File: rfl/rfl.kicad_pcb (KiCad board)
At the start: 4 copper layers, 20 x 30 mm, 35 parts, among them J1 636101111001, J2 Conn_01x09, J801 629722000214, J802 swd, U1 SX1281, U2 STM32G0B1KETxN, U3 TPS7A19, U801 USBLC6-2SC6, Y1 52MHz

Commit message: before switch
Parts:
- added C15: C, Capacitor_SMD:C_0402_1005Metric, F.Cu at (176.8, 87.3)
- added R5: R, Resistor_SMD:R_0402_1005Metric, F.Cu at (182.7, 76.5)
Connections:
- U2 pad 24: /swdclk -> /swdio
- U2 pad 25: /swdio -> /swdclk
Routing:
- net /nreset: track 8.20 -> 13.2 mm, vias 1 -> 2
- net /swdclk: track 6.42 -> 10.9 mm
- net /swdio: track 7.61 -> 8.32 mm
- net +3.3V: track 11.3 -> 11.0 mm, vias 11 -> 12
- net GND: vias 107 -> 104

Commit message: v2 with rf switch wip
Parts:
- removed C11, C12: C, Capacitor_SMD:C_0402_1005Metric
- removed L3, L4: L, Inductor_SMD:L_0402_1005Metric
- added C8: C, Capacitor_SMD:C_0603_1608Metric, F.Cu at (210.5, 77.7)
- added D3: D_TVS, Diode_SMD:D_0402_1005Metric, F.Cu at (218.0, 91.7)
- added D4: D_TVS, Diode_SMD:D_0402_1005Metric, F.Cu at (221.9, 91.7)
- added D5: D_TVS, Diode_SMD:D_0402_1005Metric, F.Cu at (210.0, 91.7)
- added D6: D_TVS, Diode_SMD:D_0402_1005Metric, F.Cu at (214.1, 91.7)
- added FL1: 2450FM07D0034001T, rfl-lib-fp:2450FM07D0034001T, F.Cu at (214.2, 77.5)
- added J3: 636101111001, Connector_Coaxial:U.FL_Hirose_U.FL-R-SMT-1_Vertical, F.Cu at (211.5, 69.8)
- added R10: R, Resistor_SMD:R_0402_1005Metric, F.Cu at (227.7, 91.7)
- added R11: R, Resistor_SMD:R_0402_1005Metric, F.Cu at (219.9, 91.7)
- added R6: R, Resistor_SMD:R_0402_1005Metric, F.Cu at (210.1, 75.5)
- added R7: R, Resistor_SMD:R_0402_1005Metric, F.Cu at (210.1, 76.5)
- added R8: R, Resistor_SMD:R_0402_1005Metric, F.Cu at (216.0, 91.7)
- added R9: R, Resistor_SMD:R_0402_1005Metric, F.Cu at (212.0, 91.7)
- added U4: SE2431L, Package_DFN_QFN:QFN-24-1EP_3x4mm_P0.4mm_EP1.65x2.65mm, F.Cu at (213.7, 74.5)
- J2: value Conn_01x09 -> Conn_01x14; footprint Connector_PinHeader_2.54mm:PinHeader_1x09_P2.54mm_Horizontal -> rfl-lib-fp:PinHeader_2x07_P2.54mm_Edge
- moved J801 50.1 mm to (223.9, 71.7), turned to 180 degrees
- moved R802 49.1 mm to (225.4, 77.7), turned to 90 degrees
- moved C15 49.1 mm to (225.7, 91.7), turned to 180 degrees
- moved C10 48.1 mm to (228.2, 90.3), turned to -90 degrees
- moved C14 47.4 mm to (225.4, 79.7), turned to -90 degrees
- moved D2 47.0 mm to (217.7, 78.0)
- moved R4 47.0 mm to (218.6, 79.0)
- moved D1 46.8 mm to (217.6, 76.0)
- moved R3 46.8 mm to (218.5, 77.0)
- moved C1 46.5 mm to (217.8, 83.2), turned to -90 degrees
- moved R2 46.4 mm to (217.3, 86.0), turned to 0 degrees
- moved C13 46.2 mm to (223.7, 91.7), turned to 180 degrees
- moved U2 45.8 mm to (223.8, 85.9), turned to 90 degrees
- moved D101 45.4 mm to (227.9, 78.8), turned to 90 degrees
- moved C5 45.4 mm to (215.9, 84.1), turned to 180 degrees
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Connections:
- C10 pad 1: Net-(C10-Pad1) -> GND
- C10 pad 2: GND -> /d3
- C6 pad 1: Net-(U1-RFIO) -> GND
- C6 pad 2: GND -> +3.3V
- C7 pad 1: Net-(C11-Pad1) -> +3.3V
- J2 pad 1: /d1 -> Net-(D6-A2)
- J2 pad 2: VDD -> Net-(D5-A2)
- J2 pad 3: GND -> VDD
- J2 pad 4: /d2 -> VDD
- J2 pad 5: VDD -> GND
- J2 pad 7: /d3 -> unconnected-(J2-Pin_7-Pad7)
- J2 pad 8: VDD -> unconnected-(J2-Pin_8-Pad8)
- J2 pad 9: GND -> Net-(D4-A2)
- U1 pad 22: Net-(U1-RFIO) -> Net-(FL1-IN)
- U2 pad 11: /busy -> /dio2
- U2 pad 18: unconnected-(U2-PA8-Pad18) -> /antsel
- U2 pad 19: unconnected-(U2-PA9/UCPD1_DBCC1-Pad19) -> /csd
- U2 pad 21: unconnected-(U2-PA10/UCPD1_DBCC2-Pad21) -> /cps
- U2 pad 26: unconnected-(U2-PD0-Pad26) -> /d4
- U2 pad 29: unconnected-(U2-PD3-Pad29) -> /ctx
- U2 pad 8: /dio1 -> /busy
- U2 pad 9: /dio2 -> /dio1
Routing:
- net /csd: track 0.00 -> 22.2 mm, vias 0 -> 2
- net /cps: track 0.00 -> 19.7 mm, vias 0 -> 4
- net /ctx: track 0.00 -> 18.9 mm, vias 0 -> 2
- net /antsel: track 0.00 -> 18.6 mm, vias 0 -> 2
- net GND: track 16.2 -> 33.4 mm, vias 104 -> 53
- net /sx_nreset: track 10.1 -> 22.6 mm
- net Net-(U2-PB1): track 3.41 -> 13.8 mm, vias 0 -> 2
- net /d4: track 0.00 -> 9.30 mm, vias 0 -> 3
- net Net-(U2-PB15): track 3.15 -> 12.4 mm, vias 0 -> 2
- net /sck: track 8.25 -> 17.3 mm
- net /dio1: track 8.87 -> 17.5 mm
- net /nreset: track 13.2 -> 4.58 mm, vias 2 -> 1
- net Net-(D4-A2): track 0.00 -> 8.31 mm
- net /dio2: track 8.38 -> 16.3 mm
- net /dio3: track 9.35 -> 17.0 mm
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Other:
- board size 20 x 30 mm -> 20 x 28.5 mm
- board text added: "s"
- board text removed: "1"
- board text removed: "rfl v1"

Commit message: cleaned up layout
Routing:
- net /csd: track 22.2 -> 24.2 mm
- net /antsel: track 18.6 -> 19.2 mm
- net GND: vias 53 -> 63
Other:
- board text added: "1"
- board text added: "2"
- board text added: "3 *"
- board text added: "4"
- board text added: "a1"
- board text added: "a2"
- board text added: "rfl v1.1 june 26"

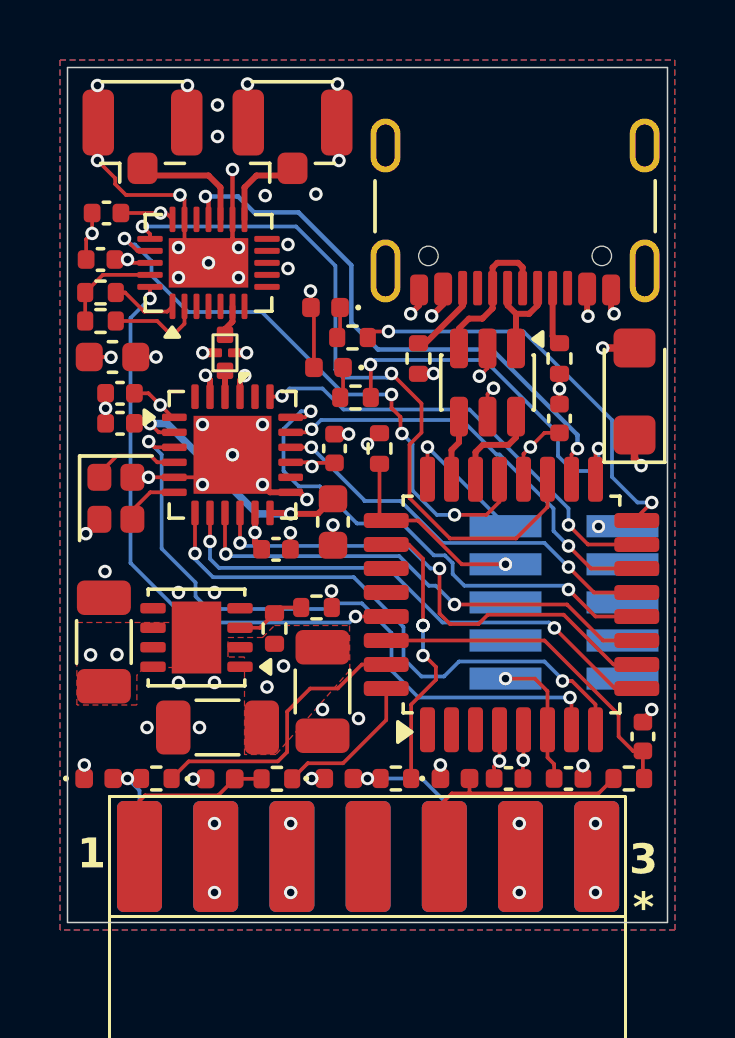
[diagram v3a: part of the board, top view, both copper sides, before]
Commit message: fixed edge cleareance
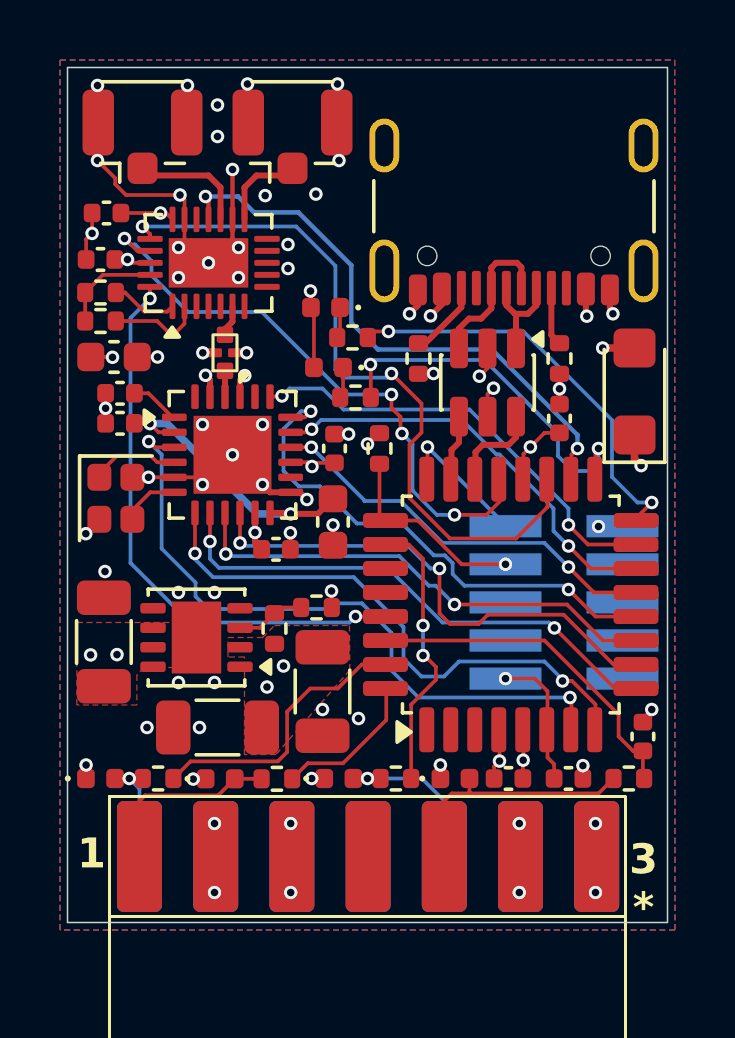
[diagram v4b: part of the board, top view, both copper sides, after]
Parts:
- J801: footprint et-misc:USB_C_Receptacle_GCT_USB4105-xx-A_16P_TopMnt_Horizontal -> rfl-lib-fp:USB_C_Receptacle_GCT_USB4105-xx-A_16P_TopMnt_Horizontal
- J802: footprint et-misc:PinHeader_2x05_P1.27mm_Vertical_SMD -> Connector_PinHeader_1.27mm:PinHeader_2x05_P1.27mm_Vertical_SMD
- moved D5 0.06 mm to (210.1, 91.7)
- moved R9 0.06 mm to (212.0, 91.7)
- moved C8 0.05 mm to (210.6, 77.7)
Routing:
- net Net-(U1-VR_PA): vias 1 -> 0
- net /d4: vias 3 -> 2

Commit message: add
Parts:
- R1: value R -> 16k
- R2, R5: value R -> 10k
- R3, R4, R7: value R -> 1k2
- R6: value R -> 2k2
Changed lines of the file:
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@@
 			)
 		)
-		(property "Value" "R"
+		(property "Value" "1k2"
 			(at 0 1.17 0)
 			(layer "F.Fab")
@@
 			)
 		)
-		(property "Value" "R"
+		(property "Value" "16k"
 			(at 0 1.17 90)
 			(layer "F.Fab")
@@
 			)
 		)
-		(property "Value" "R"
+		(property "Value" "10k"
 			(at 0 1.17 90)
 			(layer "F.Fab")
@@
 			)
 		)
-		(property "Value" "R"
+		(property "Value" "1k2"
 			(at 0 1.17 0)
 			(layer "F.Fab")
@@
 			)
 		)
-		(property "Value" "R"
+		(property "Value" "2k2"
 			(at 0 1.17 0)
 			(layer "F.Fab")
@@
 			)
 		)
-		(property "Value" "R"
+		(property "Value" "1k2"
 			(at 0 1.17 0)
 			(layer "F.Fab")
@@
 			)
 		)
+		(property "PartNo" "NX2016SA-52.000000MHZ"
+			(at 0 0 270)
+			(unlocked yes)
+			(layer "F.Fab")
+			(hide yes)
+			(effects
+				(font
+					(size 1 1)
+					(thickness 0.15)
+				)
+			)
+		)
 		(property ki_fp_filters "Crystal*")
 		(sheetname "/")
@@
 			)
 		)
+		(property "PartNo" "61301421121"
+			(at 0 0 0)
+			(unlocked yes)
+			(layer "F.Fab")
+			(hide yes)
+			(effects
+				(font
+					(size 1 1)
+					(thickness 0.15)
+				)
+			)
+		)
 		(property ki_fp_filters "Connector*:*_1x??_*")
 		(sheetname "/")
@@
 			)
 		)
-		(property "Value" "R"
+		(property "Value" "10k"
 			(at 0 1.17 0)
 			(layer "F.Fab")
@@
 			(at 0 4.285 0)
 			(layer "B.SilkS")
+			(hide yes)
 			(effects
 				(font

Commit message: first working rec/send rc
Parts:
- C1: value C -> 470n
- C10: value C -> 6p8
- C13, C14, C2, C3, C4, C5, C6, C7, C8: value C -> 100n
- D3, D4, D5, D6: value D_TVS -> CPDQC3V3C-HF
- R10, R11, R8, R9: value R -> 100R
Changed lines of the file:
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@@
 			)
 		)
-		(property "Value" "C"
+		(property "Value" "100n"
 			(at 0 1.16 0)
 			(layer "F.Fab")
@@
 			)
 		)
-		(property "Value" "C"
+		(property "Value" "100n"
 			(at 0 1.16 0)
 			(layer "F.Fab")
@@
 			)
 		)
-		(property "Value" "C"
+		(property "Value" "470n"
 			(at 0 1.43 90)
 			(layer "F.Fab")
@@
 			)
 		)
-		(property "Value" "D_TVS"
+		(property "Value" "CPDQC3V3C-HF"
 			(at 0 1.17 0)
 			(layer "F.Fab")
@@
 			)
 		)
-		(property "Value" "C"
+		(property "Value" "100n"
 			(at 0 1.16 0)
 			(layer "F.Fab")
@@
 			)
 		)
-		(property "Value" "C"
+		(property "Value" "100n"
 			(at 0 1.43 0)
 			(layer "F.Fab")
@@
 			)
 		)
-		(property "Value" "C"
+		(property "Value" "100n"
 			(at 0 1.16 90)
 			(layer "F.Fab")
@@
 			)
 		)
-		(property "Value" "C"
+		(property "Value" "100n"
 			(at 0 1.16 0)
 			(layer "F.Fab")
@@
 			)
 		)
-		(property "Value" "R"
+		(property "Value" "100R"
 			(at 0 1.17 0)
 			(layer "F.Fab")
@@
 			)
 		)
-		(property "Value" "R"
+		(property "Value" "100R"
 			(at 0 1.17 0)
 			(layer "F.Fab")
@@
 			)
 		)
-		(property "Value" "C"
+		(property "Value" "100n"
 			(at 0 1.16 90)
 			(layer "F.Fab")
@@
 			)
 		)
-		(property "Value" "C"
+		(property "Value" "6p8"
 			(at 0 1.16 90)
 			(layer "F.Fab")
@@
 			)
 		)
-		(property "Value" "R"
+		(property "Value" "100R"
 			(at 0 1.17 0)
 			(layer "F.Fab")
@@
 			)
 		)
-		(property "Value" "C"
+		(property "Value" "100n"
 			(at 0 1.16 0)
 			(layer "F.Fab")
@@
 			)
 		)
-		(property "Value" "D_TVS"
+		(property "Value" "CPDQC3V3C-HF"
 			(at 0 1.17 0)
 			(layer "F.Fab")
@@
 			)
 		)
-		(property "Value" "D_TVS"
+		(property "Value" "CPDQC3V3C-HF"
 			(at 0 1.17 0)
 			(layer "F.Fab")
@@
 			)
 		)
-		(property "Value" "R"
+		(property "Value" "100R"
 			(at 0 1.17 0)
 			(layer "F.Fab")
@@
 			)
 		)
-		(property "Value" "D_TVS"
+		(property "Value" "CPDQC3V3C-HF"
 			(at 0 1.17 0)
 			(layer "F.Fab")
@@
 			)
 		)
-		(property "Value" "C"
+		(property "Value" "100n"
 			(at 0 1.16 0)
 			(layer "F.Fab")
